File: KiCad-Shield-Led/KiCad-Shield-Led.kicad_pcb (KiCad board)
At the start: 2 copper layers, 68.6 x 53.3 mm, 8 parts, among them P1 Power, P2 Analog, P3 Digital, P4 Digital, P5 CONN_01X01, P6 CONN_01X01, P7 CONN_01X01, P8 CONN_01X01

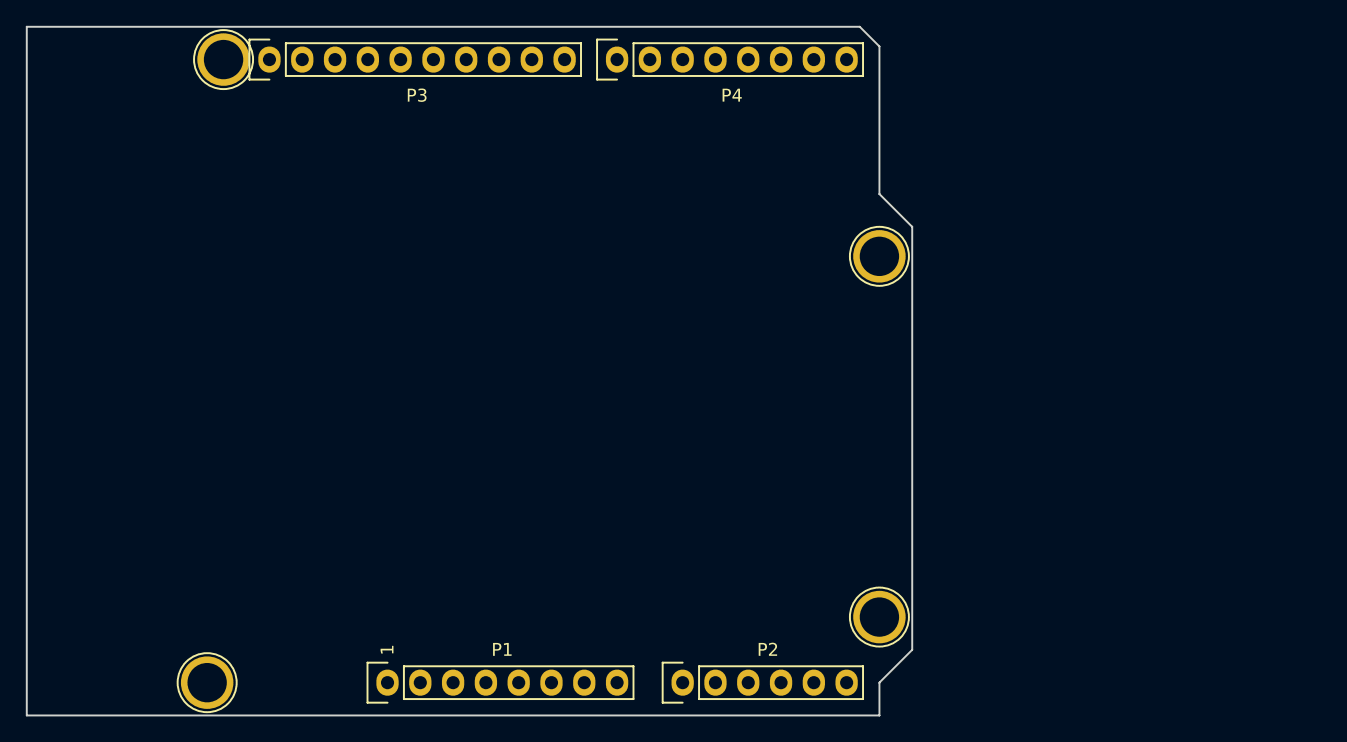
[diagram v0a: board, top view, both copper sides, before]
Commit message: Stackup before components placement
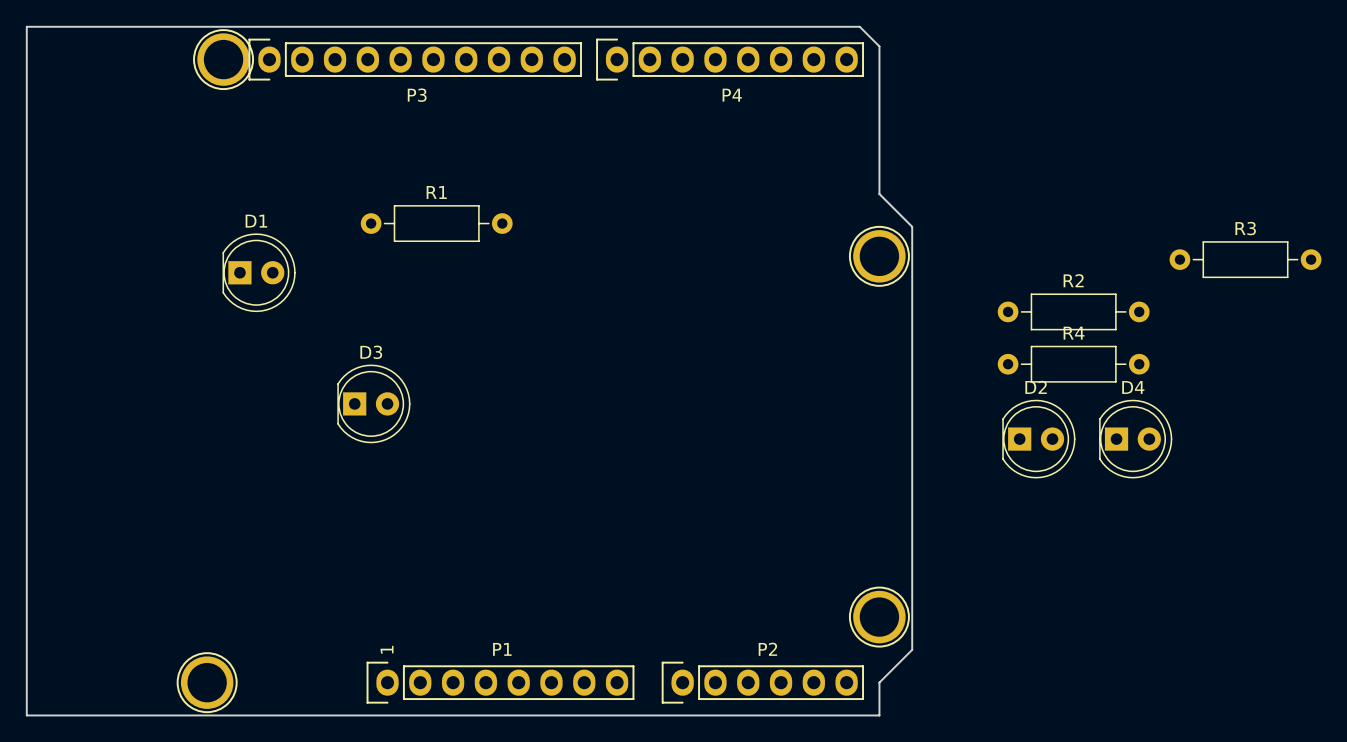
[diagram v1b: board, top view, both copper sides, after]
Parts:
- added D1: LED, LED_THT:LED_D5.0mm, F.Cu at (127.5, 92.1)
- added D2: LED, LED_THT:LED_D5.0mm, F.Cu at (187.9, 105.0)
- added D3: LED, LED_THT:LED_D5.0mm, F.Cu at (136.4, 102.2)
- added D4: LED, LED_THT:LED_D5.0mm, F.Cu at (195.4, 105.0)
- added R1: 470, Resistor_THT:R_Axial_DIN0207_L6.3mm_D2.5mm_P10.16mm_Horizontal, F.Cu at (137.7, 88.3)
- added R2: 470, Resistor_THT:R_Axial_DIN0207_L6.3mm_D2.5mm_P10.16mm_Horizontal, F.Cu at (187.0, 95.1)
- added R3: 470, Resistor_THT:R_Axial_DIN0207_L6.3mm_D2.5mm_P10.16mm_Horizontal, F.Cu at (200.3, 91.1)
- added R4: 470, Resistor_THT:R_Axial_DIN0207_L6.3mm_D2.5mm_P10.16mm_Horizontal, F.Cu at (187.0, 99.2)
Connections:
- P3 pad 6: /12(MISO) -> /LED1
- P3 pad 7: /11(**/MOSI) -> /LED2
- P3 pad 8: /10(**/SS) -> /LED3
- P3 pad 9: /9(**) -> /LED4
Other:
- net class Default: clearance 0.2 -> 0.8; trace_width 0.25 -> 0.8; via_dia 0.6 -> 1.2; via_drill 0.4 -> 0.8
- rule trace_clearance: 0.2 -> 0.8
